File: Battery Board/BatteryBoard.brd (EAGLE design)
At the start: 25.4 x 50.8 mm, 32 parts, among them IC1 TPS63060DSCT, J0 1725656, J1 1725669, J2 UJ2-MIBH2-4-SMT-TR, J3 MPTC-02-16-02-6.30-XX-X-V, J4 JSTPH2, Q1 IAUC60N04S6L030HATMA1, U0 STM32L031K4U6, U1 MCP73831T-2ATI_OT, U3 STM809TWX6F

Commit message: Further development
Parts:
- added J5: MPTC-02-04-02-6.30-XX-X-V-LC, MPTC-02-04-02-6.30-XX-X-V-LC:SAMTEC_MPTC-02-04-02-6.30-XX-X-V-LC
- moved J4 103.7 mm to (9.02, -6.48), flipped to the bottom, turned to 90 degrees
- moved R4 58.7 mm to (-1.91, -17.3), flipped to the bottom, turned to 180 degrees
- moved J2 58.6 mm to (-9.02, -13.3), flipped to the bottom, turned to 180 degrees
- moved R3 51.8 mm to (1.27, -16.4), flipped to the bottom, turned to 90 degrees
- moved U1 48.5 mm to (0.00, -20.3), flipped to the bottom
- moved R5 46.8 mm to (-0.89, -11.6), flipped to the bottom, turned to 270 degrees
- moved L1 45.9 mm to (-8.89, -2.67), flipped to the bottom, turned to 90 degrees
- moved R7 45.2 mm to (-3.05, -7.87), flipped to the bottom, turned to 270 degrees
- moved C8 44.6 mm to (2.29, -12.7), flipped to the bottom, turned to 180 degrees
- moved C10 42.3 mm to (2.29, -10.5), flipped to the bottom, turned to 180 degrees
- moved R6 42.3 mm to (0.13, -8.38), flipped to the bottom, turned to 0 degrees
- moved LED1 40.7 mm to (-1.65, -15.4), flipped to the bottom, turned to 90 degrees
- moved C6 40.2 mm to (5.08, -20.3), flipped to the bottom, turned to 90 degrees
- moved IC1 39.6 mm to (-2.79, -2.79), flipped to the bottom, turned to 180 degrees
- moved C9 38.2 mm to (1.14, -5.21), flipped to the bottom, turned to 270 degrees
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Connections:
- net GND: now also J5.P01_1, J5.P01_2, J5.P01_3, J5.P01_4, J5.P01_5, J5.P01_6, J5.P04_1, J5.P04_2, J5.P04_3, J5.P04_4, J5.P04_5, J5.P04_6
- net VBAT: now also J5.P03_1, J5.P03_2, J5.P03_3, J5.P03_4, J5.P03_5, J5.P03_6
- net VUSB: now also J5.P02_1, J5.P02_2, J5.P02_3, J5.P02_4, J5.P02_5, J5.P02_6
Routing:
- net VBAT: track 0.00 -> 25.4 mm, vias 0 -> 1
- net GND: track 0.00 -> 22.0 mm
- net VUSB: track 0.00 -> 7.21 mm
- net PROG: track 0.00 -> 2.22 mm
- net STAT: track 0.00 -> 2.05 mm
- net LED1: track 0.00 -> 1.90 mm
- added copper zone on layer 16, net GND
- added copper zone on layer 16, net VBAT
- added copper zone on layer 16, net VUSB
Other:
- board text added: "!RESET!"
- board text added: "3V3"
- board text added: "ADC"
- board text added: "BUTTON"
- board text added: "GND"
- board text added: "NRST"
- board text added: "SCL"
- board text added: "SDA"
- board text added: "SWCLK"
- board text added: "SWDIO"
- board text added: "SWO"

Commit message: "Round one of PCB" -Mark Paral 2021
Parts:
- moved U3 61.6 mm to (4.19, -0.13), turned to 270 degrees
- moved Q1 51.6 mm to (-1.14, 5.21)
- moved R2 38.8 mm to (-48.0, 42.4)
- moved C2 37.6 mm to (-43.2, 42.9)
- moved R1 33.1 mm to (-45.0, 38.9)
- moved J1 30.9 mm to (-8.38, 1.65), turned to 90 degrees
- moved R7 7.93 mm to (1.14, -1.14)
- moved C7 1.52 mm to (-2.29, 0.13)
- moved L1 1.52 mm to (-8.89, -4.19)
- moved IC1 1.52 mm to (-2.79, -4.32)
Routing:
- net VBAT: track 25.4 -> 50.4 mm
- net GND: track 22.0 -> 43.0 mm
- net 3V3: track 0.00 -> 10.0 mm
- net FB: track 0.00 -> 7.91 mm
- net SWITCH_IN: track 0.00 -> 6.14 mm
- net L2: track 0.00 -> 5.27 mm
- net L1: track 0.00 -> 5.16 mm
- net PROTECTION_NRST: track 0.00 -> 5.00 mm
- net PG: track 0.00 -> 4.03 mm
- net VAUX: track 0.00 -> 3.57 mm

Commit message: Further PCB Routing
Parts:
- moved J5 66.0 mm to (0.76, -33.0)
- moved J3 65.8 mm to (-1.02, 32.8)
- moved C3 58.0 mm to (-2.92, 11.3), turned to 270 degrees
- moved C4 57.9 mm to (-0.89, 11.3), turned to 270 degrees
- moved FB0 57.8 mm to (1.14, 11.3), turned to 90 degrees
- moved C2 57.6 mm to (4.45, 10.5), turned to 180 degrees
- moved C0 55.6 mm to (4.45, 12.8), turned to 180 degrees
- moved R2 50.3 mm to (-8.38, 11.4), turned to 90 degrees
- moved R0 50.2 mm to (4.45, 15.2), turned to 180 degrees
- moved R1 47.6 mm to (-6.10, 11.4), turned to 270 degrees
- moved U0 47.1 mm to (-0.76, 17.8), turned to 90 degrees
- moved C1 43.2 mm to (-5.21, 18.9), turned to 270 degrees
- moved LED1 0.76 mm to (-2.41, -15.4)
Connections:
- net GND: now also Q1.6; no longer C0.2, C1.2, C2.2, C3.2, C4.2, J2.MH1, J2.MH2, J2.MH3, J2.MH4, R2.1
- net GND_OUT: now also C0.2, C1.2, C2.2, C3.2, C4.2, Q1.7, R2.1
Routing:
- net GND: track 43.0 -> 80.3 mm, vias 0 -> 4
- net GND_OUT: track 0.00 -> 35.3 mm, vias 0 -> 10
- net VBAT: track 50.4 -> 60.0 mm, vias 1 -> 2
- net 3V3: track 10.0 -> 19.2 mm
- net BATT_MEAS: track 0.00 -> 8.58 mm
- net VDDA: track 0.00 -> 7.23 mm
- net BOOT0: track 0.00 -> 2.34 mm
- net LED1: track 1.90 -> 2.66 mm
- net VUSB: track 7.21 -> 6.45 mm
- added copper zone on layer 16, net 3V3
- added copper zone on layer 1, net GND
- added copper zone on layer 1, net GND_OUT
- added copper zone on layer 1, net VBAT

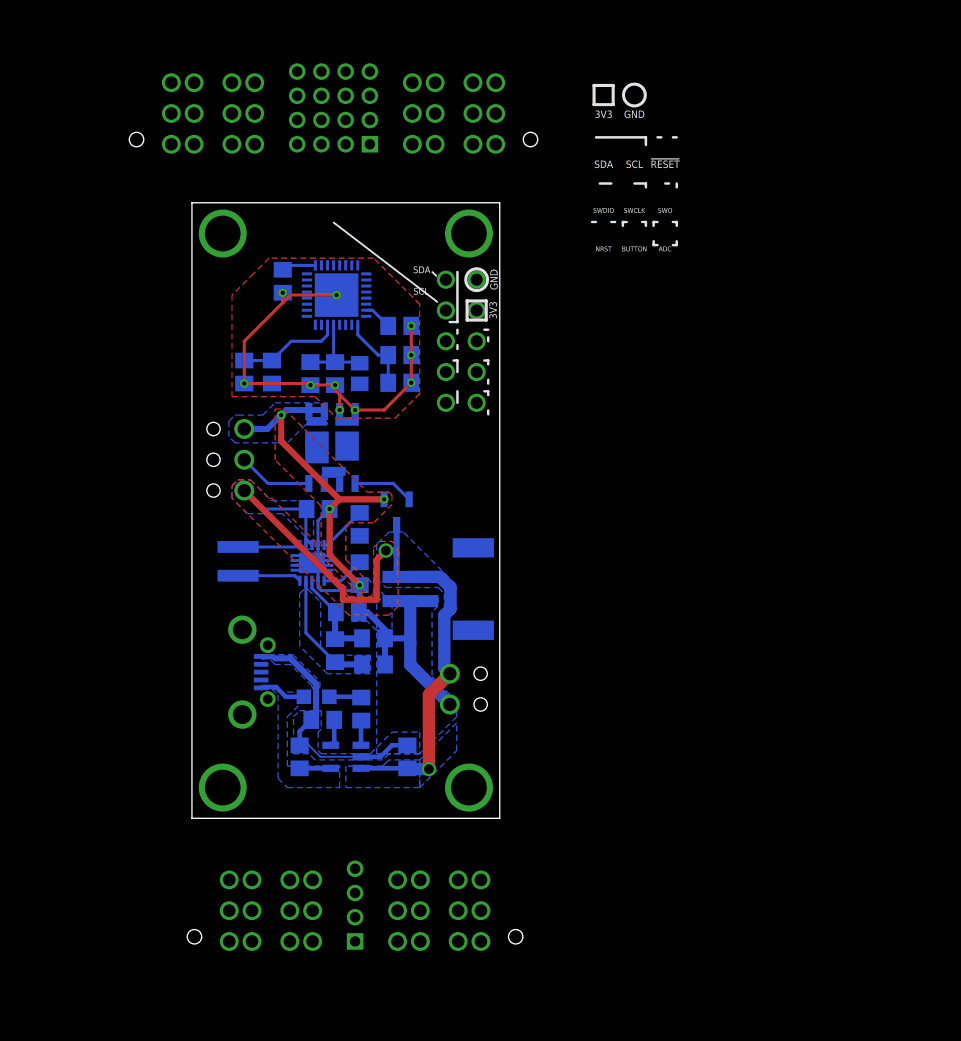
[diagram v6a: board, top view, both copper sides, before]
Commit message: Finished Schematic Pin Connections
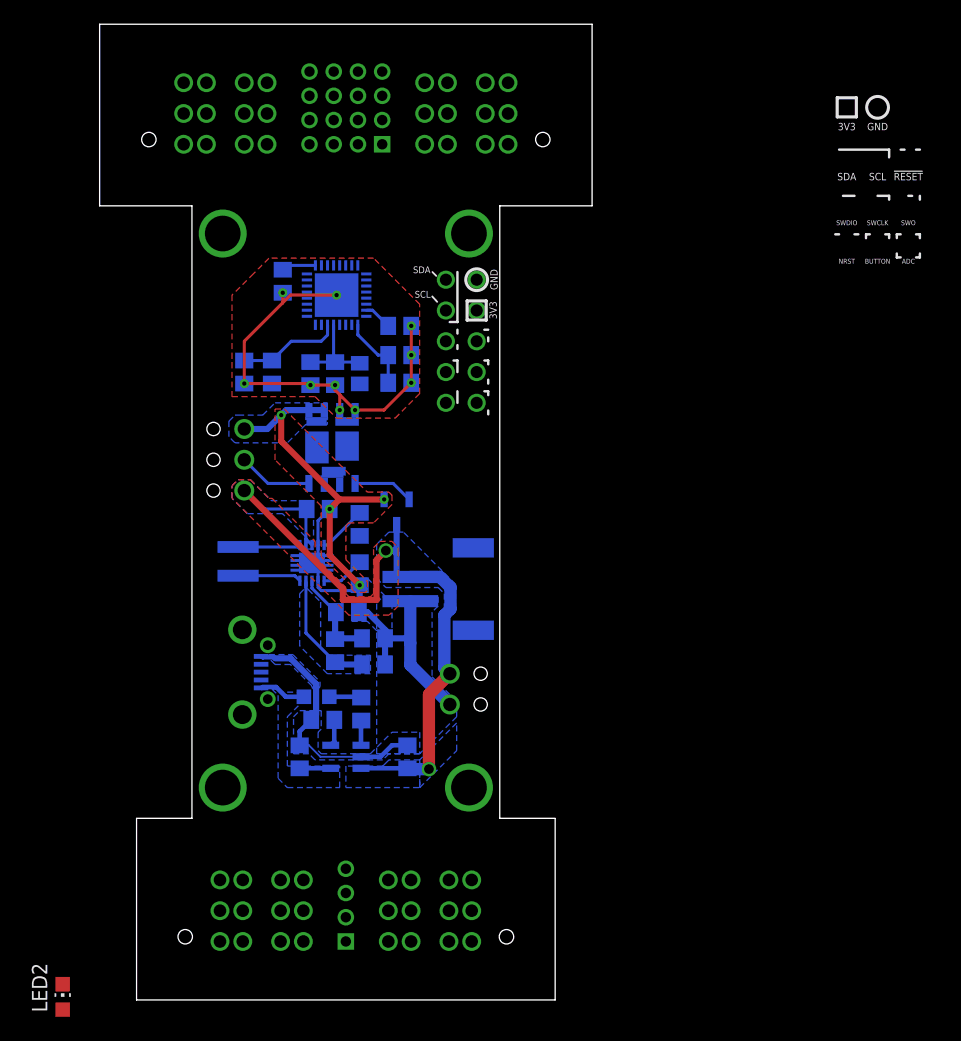
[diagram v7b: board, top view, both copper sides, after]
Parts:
- added LED2: Blue, led:CHIP-LED0805
- moved J3 1.02 mm to (0.00, 32.8)
- moved J5 0.76 mm to (0.00, -33.0)
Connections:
- removed net P03: J3.P03_1, J3.P03_2, J3.P03_3, J3.P03_4, J3.P03_5, J3.P03_6
- new net PA15: J3.D02, U0.25
- new net PA4: J3.B03, U0.10
- new net PA5: J3.B04, U0.11
- new net PA6: J3.C01, U0.12
- new net PA7: J3.C02, U0.13
- new net PB0: J3.C03, U0.14
- new net PB1: J3.C04, U0.15
- new net PB2: J3.D01, U0.16
- new net PB3: J3.D03, U0.26
- new net PB4: J3.D04, U0.27
- new net PB5: J5.B01, U0.28
- new net PB6: J5.A01, U0.29
- new net PB7: LED2.C, U0.30
- net 3V3: now also J3.P03_1, J3.P03_2, J3.P03_3, J3.P03_4, J3.P03_5, J3.P03_6
- net GND: now also LED2.A
- net I2C_SCL: now also J3.A04, J5.D01
- net I2C_SDA: now also J3.A03, J5.C01
- net NRST: now also J3.B01
- net SWCLK: now also J3.A01
- net SWDIO: now also J3.A02
- net TX: now also J3.B02
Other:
- board size 25.4 x 50.8 mm -> 40.6 x 80.5 mm

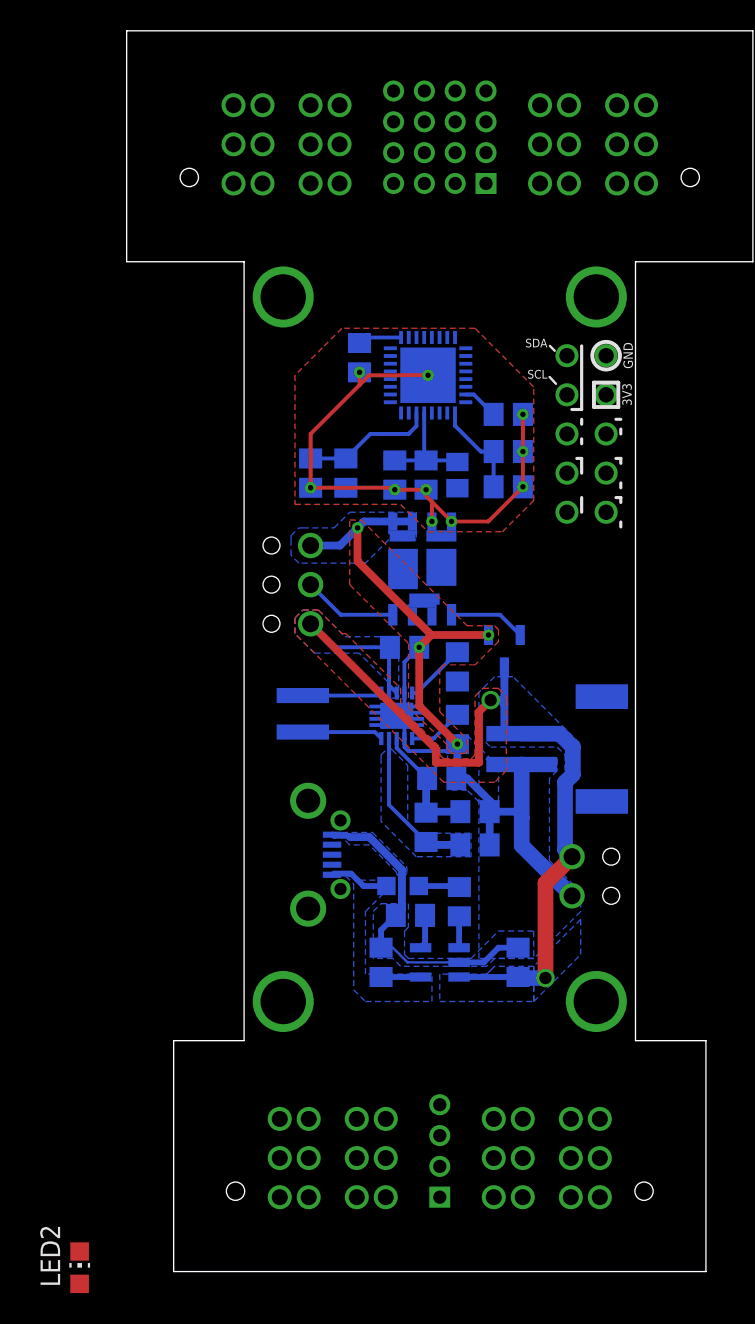
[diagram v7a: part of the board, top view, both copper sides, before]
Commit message: Routed everything besides the pinheaders
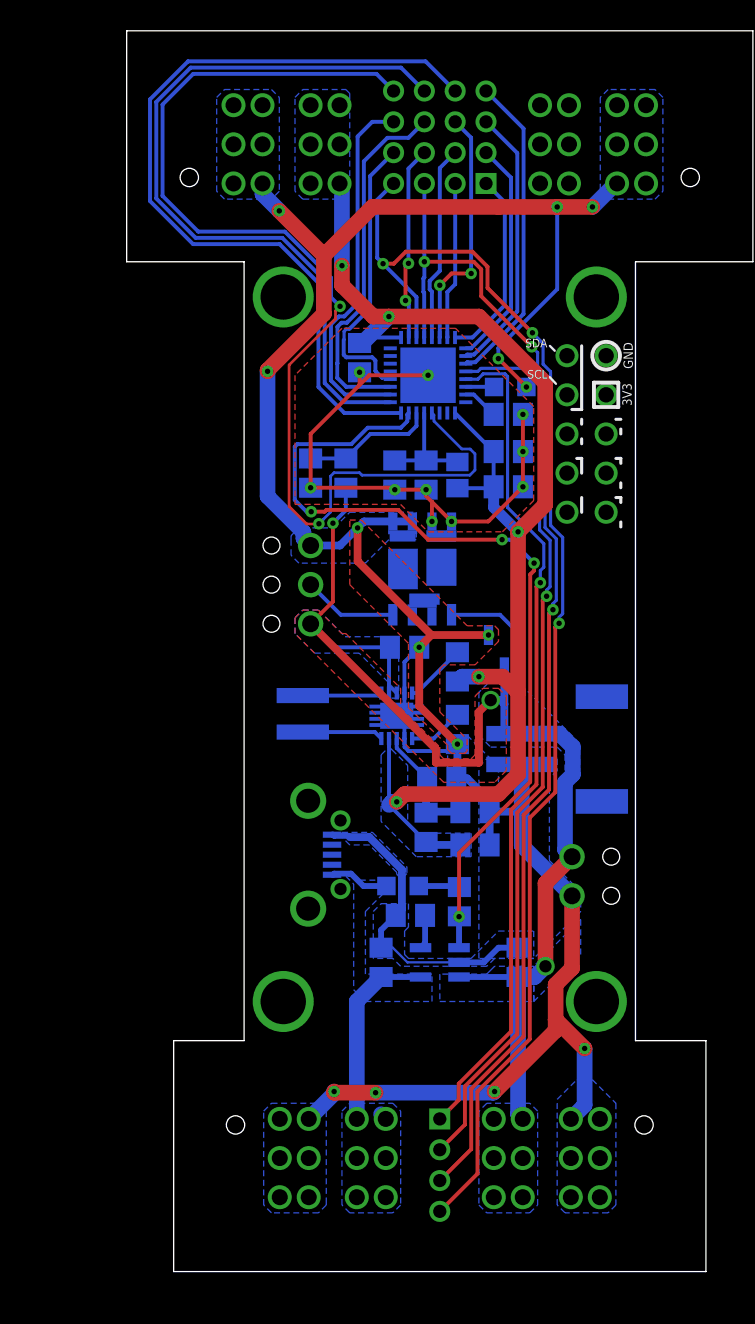
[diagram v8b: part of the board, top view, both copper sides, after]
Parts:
- moved LED2 63.6 mm to (4.57, 17.0), flipped to the bottom, turned to 270 degrees
- turned J5 to 180 degrees
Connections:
- removed net PA7: J3.C02, U0.13
- removed net PB0: J3.C03, U0.14
- removed net PB1: J3.C04, U0.15
- removed net PB2: J3.D01, U0.16
- new net PA11: J3.B02, U0.21
- new net PA12: J3.C02, U0.22
- new net PA8: J3.B03, U0.18
- net NRST: now also J3.D04; no longer J3.B01
- net PA15: now also J3.B01; no longer J3.D02
- net PA4: now also J3.C04; no longer J3.B03
- net PA5: now also J3.C03; no longer J3.B04
- net PA6: now also J3.B04; no longer J3.C01
- net PB3: now also J3.C01; no longer J3.D03
- net PB4: now also J3.D01; no longer J3.D04
- net RX: now also J3.D03
- net TX: now also J3.D02; no longer J3.B02
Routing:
- net GND: track 80.3 -> 179.5 mm, vias 4 -> 14
- net I2C_SCL: track 0.00 -> 85.6 mm, vias 0 -> 3
- net I2C_SDA: track 0.00 -> 78.3 mm, vias 0 -> 3
- net NRST: track 0.00 -> 72.4 mm, vias 0 -> 2
- net 3V3: track 19.2 -> 90.8 mm, vias 0 -> 5
- net PB5: track 0.00 -> 58.5 mm, vias 0 -> 1
- net PB6: track 0.00 -> 54.9 mm, vias 0 -> 1
- net STAT: track 2.05 -> 56.4 mm, vias 0 -> 4
- net TX: track 0.00 -> 54.2 mm
- net RX: track 0.00 -> 49.8 mm
- net PA4: track 0.00 -> 23.7 mm
- net PA5: track 0.00 -> 23.6 mm
- net PB4: track 0.00 -> 20.6 mm
- net VBAT: track 60.0 -> 78.9 mm, vias 2 -> 3
- net PA6: track 0.00 -> 18.8 mm
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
